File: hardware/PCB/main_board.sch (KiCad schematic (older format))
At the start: 0 parts

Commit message: update pcb,
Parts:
- added J?: TTL_UART, symbol Connector_Generic:Conn_01x03
- added J?: DPS1_UART, symbol Connector_Generic:Conn_01x03
- added J?: DPS2_UART, symbol Connector_Generic:Conn_01x03
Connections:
- net GND: now also J?.1 (Pin_1), J?.1 (Pin_1), J?.1 (Pin_1)
- new net licheepi_nano/UART0_RX: J?.3 (Pin_3)
- new net licheepi_nano/UART0_TX: J?.2 (Pin_2)
- new net licheepi_nano/UART1_RX: J?.3 (Pin_3)
- new net licheepi_nano/UART1_TX: J?.2 (Pin_2)
- new net licheepi_nano/UART2_RX: J?.3 (Pin_3)
- new net licheepi_nano/UART2_TX: J?.2 (Pin_2)
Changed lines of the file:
@@
 $Descr A4 11693 8268
 encoding utf-8
-Sheet 1 4
+Sheet 1 5
 Title ""
 Date ""
@@
 $EndDescr
 $Comp
-L customized_power:+5V #PWR?
+L customized_power:+5V #PWR0101
 U 1 1 5E8767E8
 P 950 1000
-F 0 "#PWR?" H 950 850 50  0001 C CNN
+F 0 "#PWR0101" H 950 850 50  0001 C CNN
 F 1 "+5V" H 965 1173 50  0000 C CNN
 F 2 "" H 950 1000 50  0001 C CNN
@@
 $EndComp
 $Comp
-L power:GND #PWR?
+L power:GND #PWR0102
 U 1 1 5E876DA9
 P 950 1300
-F 0 "#PWR?" H 950 1050 50  0001 C CNN
+F 0 "#PWR0102" H 950 1050 50  0001 C CNN
 F 1 "GND" H 955 1127 50  0000 C CNN
 F 2 "" H 950 1300 50  0001 C CNN
@@
 	1    0    0    -1
 $EndComp
-$Sheet
-S 4500 2400 1400 1050
+Entry Wire Line
+	3450 3150 3550 3050
+Entry Wire Line
+	3450 3050 3550 2950
+Entry Wire Line
+	3450 2950 3550 2850
+Entry Wire Line
+	3450 2850 3550 2750
+Entry Wire Line
+	3450 2750 3550 2650
+Entry Wire Line
+	3450 2650 3550 2550
+Wire Bus Line
+	3550 2300 4150 2300
+Entry Wire Line
+	4150 2550 4250 2650
+Entry Wire Line
+	4150 2650 4250 2750
+Entry Wire Line
+	4150 2750 4250 2850
+Entry Wire Line
+	4150 2850 4250 2950
+Entry Wire Line
+	4150 2950 4250 3050
+Entry Wire Line
+	4150 3050 4250 3150
+Wire Wire Line
+	4250 2650 4800 2650
+Wire Wire Line
+	4250 2750 4800 2750
+Wire Wire Line
+	4250 2850 4800 2850
+Wire Wire Line
+	4250 2950 4800 2950
+Wire Wire Line
+	4250 3050 4800 3050
+Wire Wire Line
+	4250 3150 4800 3150
+Wire Wire Line
+	2900 3150 3450 3150
+Wire Wire Line
+	2900 2650 3450 2650
+Wire Wire Line
+	2900 2750 3450 2750
+Wire Wire Line
+	2900 2850 3450 2850
+Wire Wire Line
+	2900 2950 3450 2950
+Wire Wire Line
+	2900 3050 3450 3050
+$Sheet
+S 1500 2400 1400 1050
+U 5E8B2717
+F0 "wifi" 50
+F1 "wifi.sch" 50
+F2 "SDC1_D2" B R 2900 3050 50
+F3 "SDC1_D1" B R 2900 2950 50
+F4 "SDC1_D0" B R 2900 2850 50
+F5 "SDC1_CLK" B R 2900 2750 50
+F6 "SDC1_CMD" B R 2900 2650 50
+F7 "SDC1_D3" B R 2900 3150 50
+$EndSheet
+Text Label 3000 2650 0    50   ~ 0
+SDC1_CMD
+Text Label 3000 2750 0    50   ~ 0
+SDC1_CLK
+Text Label 3000 2850 0    50   ~ 0
+SDC1_D0
+Text Label 3000 2950 0    50   ~ 0
+SDC1_D1
+Text Label 3000 3050 0    50   ~ 0
+SDC1_D2
+Text Label 3000 3150 0    50   ~ 0
+SDC1_D3
+Text Label 4350 2650 0    50   ~ 0
+SDC1_CMD
+Text Label 4350 2750 0    50   ~ 0
+SDC1_CLK
+Text Label 4350 2850 0    50   ~ 0
+SDC1_D0
+Text Label 4350 2950 0    50   ~ 0
+SDC1_D1
+Text Label 4350 3050 0    50   ~ 0
+SDC1_D2
+Text Label 4350 3150 0    50   ~ 0
+SDC1_D3
+$Sheet
+S 8450 4650 1600 1300
+U 5E91CDD8
+F0 "buzzer" 50
+F1 "buzzer.sch" 50
+F2 "BUZZER_OUTPUT" I L 8450 5150 50
+$EndSheet
+Wire Wire Line
+	7050 2600 8450 2600
+Wire Wire Line
+	7050 2800 8450 2800
+Wire Wire Line
+	7050 2900 8450 2900
+Wire Wire Line
+	7050 3000 8450 3000
+$Sheet
+S 8450 2400 1600 1050
+U 5E87CEF1
+F0 "gpio" 50
+F1 "gpio.sch" 50
+F2 "FEL" O L 8450 2600 50
+F3 "USER_BTN1" O L 8450 2800 50
+F4 "USER_BTN2" O L 8450 2900 50
+F5 "USER_BTN3" O L 8450 3000 50
+$EndSheet
+Wire Wire Line
+	7050 3900 7700 3900
+Wire Wire Line
+	7700 3900 7700 5150
+Wire Wire Line
+	7700 5150 8450 5150
+$Sheet
+S 4800 2400 2250 2250
 U 5E87A116
 F0 "licheepi_nano" 50
 F1 "licheepi_nano.sch" 50
-$EndSheet
-$Sheet
-S 6850 2400 1600 1050
-U 5E87CEF1
-F0 "gpio" 50
-F1 "gpio.sch" 50
-$EndSheet
-$Sheet
-S 2200 2400 1400 1050
-U 5E8B2717
-F0 "wifi" 50
-F1 "wifi.sch" 50
-$EndSheet
+F2 "SDC1_D2" B L 4800 3050 50
+F3 "SDC1_D1" B L 4800 2950 50
+F4 "SDC1_D0" B L 4800 2850 50
+F5 "SDC1_CLK" B L 4800 2750 50
+F6 "SDC1_CMD" B L 4800 2650 50
+F7 "SDC1_D3" B L 4800 3150 50
+F8 "FEL_ENABLE" I R 7050 2600 50
+F9 "PE2" I R 7050 2800 50
+F10 "PE3" I R 7050 2900 50
+F11 "PE4" I R 7050 3000 50
+F12 "PE5" O R 7050 3900 50
+F13 "UART0_TX" I L 4800 3450 50
+F14 "UART0_RX" I L 4800 3550 50
+F15 "UART1_TX" I L 4800 3800 50
+F16 "UART1_RX" I L 4800 3900 50
+F17 "UART2_RX" I L 4800 4250 50
+F18 "UART2_TX" I L 4800 4150 50
+$EndSheet
+$Comp
+L Connector_Generic:Conn_01x03 J?
+U 1 1 5E949A7D
+P 3750 3450
+F 0 "J?" H 3668 3767 50  0000 C CNN
+F 1 "TTL_UART" H 3668 3676 50  0000 C CNN
+F 2 "" H 3750 3450 50  0001 C CNN
+F 3 "~" H 3750 3450 50  0001 C CNN
+	1    3750 3450
+	-1   0    0    -1
+$EndComp
+$Comp
+L power:GND #PWR?
+U 1 1 5E94A27E
+P 4200 3350
+F 0 "#PWR?" H 4200 3100 50  0001 C CNN
+F 1 "GND" V 4205 3222 50  0000 R CNN
+F 2 "" H 4200 3350 50  0001 C CNN
+F 3 "" H 4200 3350 50  0001 C CNN
+	1    4200 3350
+	0    -1   -1   0
+$EndComp
+Wire Wire Line
+	3950 3350 4200 3350
+Wire Wire Line
+	3950 3450 4800 3450
+Wire Wire Line
+	3950 3550 4800 3550
+$Comp
+L Connector_Generic:Conn_01x03 J?
+U 1 1 5E94B27C
+P 3750 3800
+F 0 "J?" H 3829 3842 50  0000 L CNN
+F 1 "DPS1_UART" H 3829 3751 50  0000 L CNN
+F 2 "" H 3750 3800 50  0001 C CNN
+F 3 "~" H 3750 3800 50  0001 C CNN
+	1    3750 3800
+	-1   0    0    -1
+$EndComp
+$Comp
+L power:GND #PWR?
+U 1 1 5E94B286
+P 4200 3700
+F 0 "#PWR?" H 4200 3450 50  0001 C CNN
+F 1 "GND" V 4205 3572 50  0000 R CNN
+F 2 "" H 4200 3700 50  0001 C CNN
+F 3 "" H 4200 3700 50  0001 C CNN
+	1    4200 3700
+	0    -1   -1   0
+$EndComp
+Wire Wire Line
+	3950 3700 4200 3700
+Wire Wire Line
+	3950 3800 4800 3800
+Wire Wire Line
+	3950 3900 4800 3900
+$Comp
+L Connector_Generic:Conn_01x03 J?
+U 1 1 5E94C724
+P 3750 4150
+F 0 "J?" H 3829 4192 50  0000 L CNN
+F 1 "DPS2_UART" H 3829 4101 50  0000 L CNN
+F 2 "" H 3750 4150 50  0001 C CNN
+F 3 "~" H 3750 4150 50  0001 C CNN
+	1    3750 4150
+	-1   0    0    -1
+$EndComp
+$Comp
+L power:GND #PWR?
+U 1 1 5E94C72E
+P 4200 4050
+F 0 "#PWR?" H 4200 3800 50  0001 C CNN
+F 1 "GND" V 4205 3922 50  0000 R CNN
+F 2 "" H 4200 4050 50  0001 C CNN
+F 3 "" H 4200 4050 50  0001 C CNN
+	1    4200 4050
+	0    -1   -1   0
+$EndComp
+Wire Wire Line
+	3950 4050 4200 4050
+Wire Wire Line
+	3950 4150 4800 4150
+Wire Wire Line
+	3950 4250 4800 4250
+Wire Bus Line
+	3550 2300 3550 3050
+Wire Bus Line
+	4150 2300 4150 3050
 $EndSCHEMATC

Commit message: update before change,
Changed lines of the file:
@@
 $Descr A4 11693 8268
 encoding utf-8
-Sheet 1 5
+Sheet 1 6
 Title ""
 Date ""
@@
 SDC1_D3
 $Sheet
-S 8450 4650 1600 1300
+S 8400 3700 950  800
 U 5E91CDD8
 F0 "buzzer" 50
 F1 "buzzer.sch" 50
-F2 "BUZZER_OUTPUT" I L 8450 5150 50
+F2 "BUZZER_OUTPUT" I L 8400 4200 50
 $EndSheet
 Wire Wire Line
@@
 	7050 3900 7700 3900
 Wire Wire Line
-	7700 3900 7700 5150
-Wire Wire Line
-	7700 5150 8450 5150
-$Sheet
-S 4800 2400 2250 2250
+	7700 3900 7700 4200
+Wire Wire Line
+	7700 4200 8400 4200
+$Sheet
+S 4800 2400 2250 3200
 U 5E87A116
 F0 "licheepi_nano" 50
@@
 F17 "UART2_RX" I L 4800 4250 50
 F18 "UART2_TX" I L 4800 4150 50
+F19 "I2C0-SCK" B R 7050 4650 50
+F20 "I2C0-SDA" B R 7050 4750 50
+F21 "SPI0_CS" I R 7050 5100 50
+F22 "SPI0_MOSI" I R 7050 5200 50
+F23 "SPI0_CLK" I R 7050 5300 50
+F24 "SPI0_MISO" I R 7050 5400 50
 $EndSheet
 $Comp
@@
 	-1   0    0    -1
 $EndComp
+Wire Wire Line
+	3950 3450 4800 3450
+Wire Wire Line
+	3950 3550 4800 3550
+$Comp
+L Connector_Generic:Conn_01x03 J?
+U 1 1 5E94B27C
+P 3750 3800
+F 0 "J?" H 3829 3842 50  0000 L CNN
+F 1 "DPS1_UART" H 3829 3751 50  0000 L CNN
+F 2 "" H 3750 3800 50  0001 C CNN
+F 3 "~" H 3750 3800 50  0001 C CNN
+	1    3750 3800
+	-1   0    0    -1
+$EndComp
+$Comp
+L power:GND #PWR?
+U 1 1 5E94B286
+P 4200 3700
+F 0 "#PWR?" H 4200 3450 50  0001 C CNN
+F 1 "GND" V 4205 3572 50  0000 R CNN
+F 2 "" H 4200 3700 50  0001 C CNN
+F 3 "" H 4200 3700 50  0001 C CNN
+	1    4200 3700
+	0    -1   -1   0
+$EndComp
+Wire Wire Line
+	3950 3700 4200 3700
+Wire Wire Line
+	3950 3800 4800 3800
+Wire Wire Line
+	3950 3900 4800 3900
+$Comp
+L Connector_Generic:Conn_01x03 J?
+U 1 1 5E94C724
+P 3750 4150
+F 0 "J?" H 3829 4192 50  0000 L CNN
+F 1 "DPS2_UART" H 3829 4101 50  0000 L CNN
+F 2 "" H 3750 4150 50  0001 C CNN
+F 3 "~" H 3750 4150 50  0001 C CNN
+	1    3750 4150
+	-1   0    0    -1
+$EndComp
+$Comp
+L power:GND #PWR?
+U 1 1 5E94C72E
+P 4200 4050
+F 0 "#PWR?" H 4200 3800 50  0001 C CNN
+F 1 "GND" V 4205 3922 50  0000 R CNN
+F 2 "" H 4200 4050 50  0001 C CNN
+F 3 "" H 4200 4050 50  0001 C CNN
+	1    4200 4050
+	0    -1   -1   0
+$EndComp
+Wire Wire Line
+	3950 4050 4200 4050
+Wire Wire Line
+	3950 4150 4800 4150
+Wire Wire Line
+	3950 4250 4800 4250
+$Sheet
+S 9300 5000 950  1150
+U 5E8E2BE1
+F0 "terminals" 50
+F1 "terminals.sch" 50
+$EndSheet
+Wire Bus Line
+	7650 6150 8500 6150
+Wire Bus Line
+	8500 6150 8500 5050
+Entry Wire Line
+	7550 4650 7650 4750
+Entry Wire Line
+	7550 4750 7650 4850
+Entry Wire Line
+	7550 5100 7650 5200
+Entry Wire Line
+	7550 5200 7650 5300
+Entry Wire Line
+	7550 5300 7650 5400
+Entry Wire Line
+	7550 5400 7650 5500
+Wire Wire Line
+	7050 4650 7550 4650
+Wire Wire Line
+	7050 4750 7550 4750
+Wire Wire Line
+	7050 5100 7550 5100
+Wire Wire Line
+	7050 5200 7550 5200
+Wire Wire Line
+	7050 5300 7550 5300
+Wire Wire Line
+	7050 5400 7550 5400
+Text Label 7500 4650 2    50   ~ 0
+I2C0-SCK
+Text Label 7500 4750 2    50   ~ 0
+I2C0-SDA
+Text Label 7500 5100 2    50   ~ 0
+SPI0_CS
+Text Label 7500 5200 2    50   ~ 0
+SPI0_MOSI
+Text Label 7500 5300 2    50   ~ 0
+SPI0_CLK
+Text Label 7500 5400 2    50   ~ 0
+SPI0_MISO
+Wire Bus Line
+	7650 4550 7650 6150
+Wire Bus Line
+	4150 2300 4150 3050
+Wire Bus Line
+	3550 2300 3550 3050
+Wire Wire Line
+	3950 3350 4200 3350
 $Comp
 L power:GND #PWR?
@@
 	0    -1   -1   0
 $EndComp
-Wire Wire Line
-	3950 3350 4200 3350
-Wire Wire Line
-	3950 3450 4800 3450
-Wire Wire Line
-	3950 3550 4800 3550
-$Comp
-L Connector_Generic:Conn_01x03 J?
-U 1 1 5E94B27C
-P 3750 3800
-F 0 "J?" H 3829 3842 50  0000 L CNN
-F 1 "DPS1_UART" H 3829 3751 50  0000 L CNN
-F 2 "" H 3750 3800 50  0001 C CNN
-F 3 "~" H 3750 3800 50  0001 C CNN
-	1    3750 3800
-	-1   0    0    -1
-$EndComp
-$Comp
-L power:GND #PWR?
-U 1 1 5E94B286
-P 4200 3700
-F 0 "#PWR?" H 4200 3450 50  0001 C CNN
-F 1 "GND" V 4205 3572 50  0000 R CNN
-F 2 "" H 4200 3700 50  0001 C CNN
-F 3 "" H 4200 3700 50  0001 C CNN
-	1    4200 3700
-	0    -1   -1   0
-$EndComp
-Wire Wire Line
-	3950 3700 4200 3700
-Wire Wire Line
-	3950 3800 4800 3800
-Wire Wire Line
-	3950 3900 4800 3900
-$Comp
-L Connector_Generic:Conn_01x03 J?
-U 1 1 5E94C724
-P 3750 4150
-F 0 "J?" H 3829 4192 50  0000 L CNN
-F 1 "DPS2_UART" H 3829 4101 50  0000 L CNN
-F 2 "" H 3750 4150 50  0001 C CNN
-F 3 "~" H 3750 4150 50  0001 C CNN
-	1    3750 4150
-	-1   0    0    -1
-$EndComp
-$Comp
-L power:GND #PWR?
-U 1 1 5E94C72E
-P 4200 4050
-F 0 "#PWR?" H 4200 3800 50  0001 C CNN
-F 1 "GND" V 4205 3922 50  0000 R CNN
-F 2 "" H 4200 4050 50  0001 C CNN
-F 3 "" H 4200 4050 50  0001 C CNN
-	1    4200 4050
-	0    -1   -1   0
-$EndComp
-Wire Wire Line
-	3950 4050 4200 4050
-Wire Wire Line
-	3950 4150 4800 4150
-Wire Wire Line
-	3950 4250 4800 4250
-Wire Bus Line
-	3550 2300 3550 3050
-Wire Bus Line
-	4150 2300 4150 3050
 $EndSCHEMATC

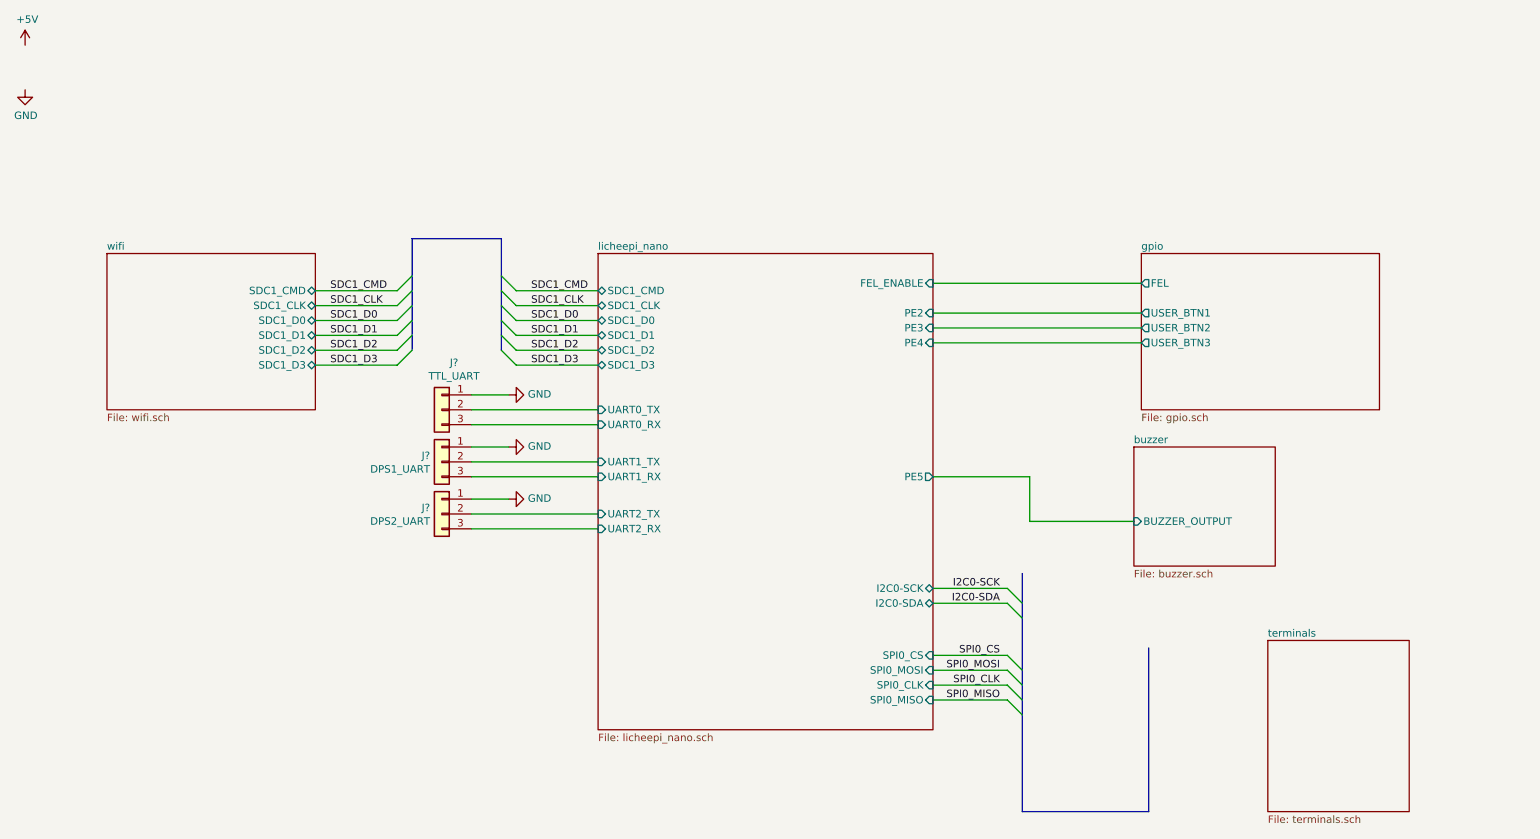
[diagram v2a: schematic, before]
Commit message: update for adding usb ttl converter,
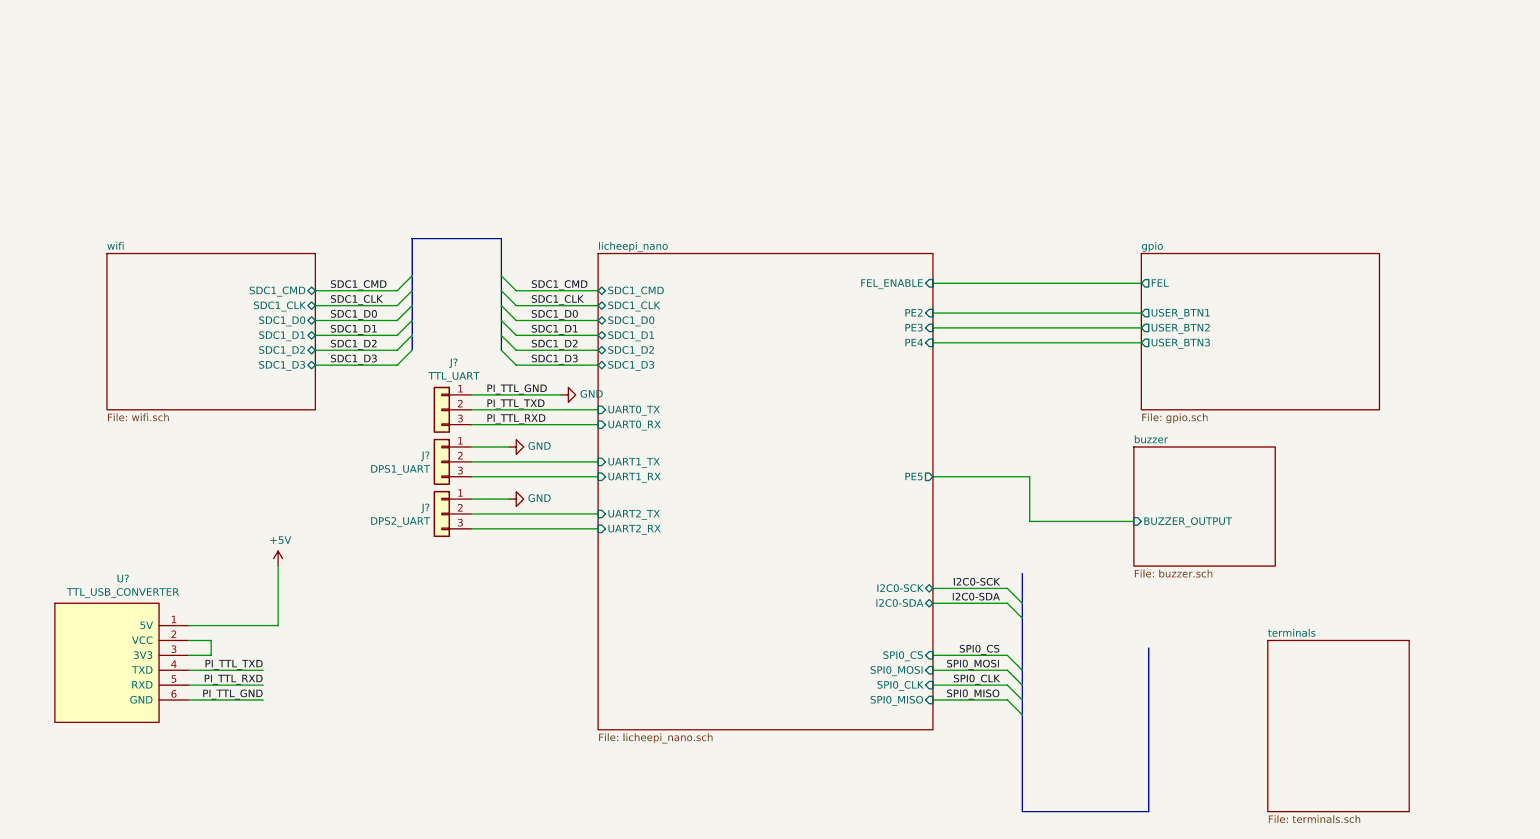
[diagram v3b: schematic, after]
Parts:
- added U?: TTL_USB_CONVERTER, footprint-lib:TTL_USB_CONVERTER, symbol taobao-components:TTL_USB_CONVERTER
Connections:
- net +5V: now also U?.1 (5V)
- net GND: now also U?.6 (GND)
- net licheepi_nano/UART0_RX renamed PI_TTL_RXD
- net PI_TTL_RXD: now also U?.5 (RXD)
- net licheepi_nano/UART0_TX renamed PI_TTL_TXD
- net PI_TTL_TXD: now also U?.4 (TXD)
- new net: U?.2 (VCC), U?.3 (3V3)
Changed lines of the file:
@@
 Comment4 ""
 $EndDescr
-$Comp
-L customized_power:+5V #PWR0101
-U 1 1 5E8767E8
-P 950 1000
-F 0 "#PWR0101" H 950 850 50  0001 C CNN
-F 1 "+5V" H 965 1173 50  0000 C CNN
-F 2 "" H 950 1000 50  0001 C CNN
-F 3 "" H 950 1000 50  0001 C CNN
-	1    950  1000
-	1    0    0    -1
-$EndComp
-$Comp
-L power:GND #PWR0102
-U 1 1 5E876DA9
-P 950 1300
-F 0 "#PWR0102" H 950 1050 50  0001 C CNN
-F 1 "GND" H 955 1127 50  0000 C CNN
-F 2 "" H 950 1300 50  0001 C CNN
-F 3 "" H 950 1300 50  0001 C CNN
-	1    950  1300
-	1    0    0    -1
-$EndComp
 Entry Wire Line
 	3450 3150 3550 3050
@@
 Text Label 7500 5400 2    50   ~ 0
 SPI0_MISO
-Wire Bus Line
-	7650 4550 7650 6150
-Wire Bus Line
-	4150 2300 4150 3050
-Wire Bus Line
-	3550 2300 3550 3050
-Wire Wire Line
-	3950 3350 4200 3350
+Wire Wire Line
+	3950 3350 4550 3350
 $Comp
 L power:GND #PWR?
 U 1 1 5E94A27E
-P 4200 3350
-F 0 "#PWR?" H 4200 3100 50  0001 C CNN
-F 1 "GND" V 4205 3222 50  0000 R CNN
-F 2 "" H 4200 3350 50  0001 C CNN
-F 3 "" H 4200 3350 50  0001 C CNN
-	1    4200 3350
+P 4550 3350
+F 0 "#PWR?" H 4550 3100 50  0001 C CNN
+F 1 "GND" V 4555 3222 50  0000 R CNN
+F 2 "" H 4550 3350 50  0001 C CNN
+F 3 "" H 4550 3350 50  0001 C CNN
+	1    4550 3350
 	0    -1   -1   0
 $EndComp
+$Comp
+L taobao-components:TTL_USB_CONVERTER U?
+U 1 1 5E991FE4
+P 1500 5150
+F 0 "U?" H 1608 5715 50  0000 C CNN
+F 1 "TTL_USB_CONVERTER" H 1608 5624 50  0000 C CNN
+F 2 "footprint-lib:TTL_USB_CONVERTER" H 1500 5150 50  0001 C CNN
+F 3 "" H 1500 5150 50  0001 C CNN
+	1    1500 5150
+	1    0    0    -1
+$EndComp
+Text Label 4050 3350 0    50   ~ 0
+PI_TTL_GND
+Text Label 4050 3450 0    50   ~ 0
+PI_TTL_TXD
+Text Label 4050 3550 0    50   ~ 0
+PI_TTL_RXD
+Text Label 2550 5400 2    50   ~ 0
+PI_TTL_GND
+Text Label 2550 5200 2    50   ~ 0
+PI_TTL_TXD
+Text Label 2550 5300 2    50   ~ 0
+PI_TTL_RXD
+Wire Wire Line
+	2050 5200 2550 5200
+Wire Wire Line
+	2050 5300 2550 5300
+Wire Wire Line
+	2050 5400 2550 5400
+$Comp
+L customized_power:+5V #PWR?
+U 1 1 5E99CA17
+P 2650 4500
+F 0 "#PWR?" H 2650 4350 50  0001 C CNN
+F 1 "+5V" H 2665 4673 50  0000 C CNN
+F 2 "" H 2650 4500 50  0001 C CNN
+F 3 "" H 2650 4500 50  0001 C CNN
+	1    2650 4500
+	1    0    0    -1
+$EndComp
+Wire Wire Line
+	2650 4500 2650 4900
+Wire Wire Line
+	2650 4900 2050 4900
+Wire Wire Line
+	2050 5000 2200 5000
+Wire Wire Line
+	2200 5000 2200 5100
+Wire Wire Line
+	2200 5100 2050 5100
+Wire Bus Line
+	3550 2300 3550 3050
+Wire Bus Line
+	4150 2300 4150 3050
+Wire Bus Line
+	7650 4550 7650 6150
 $EndSCHEMATC

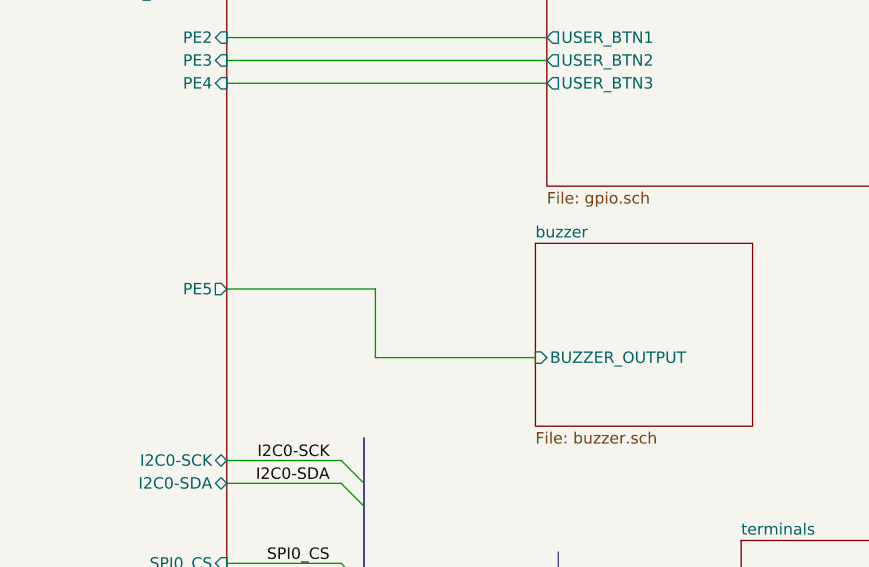
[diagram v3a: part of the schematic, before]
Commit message: sch: update buzzer connection,
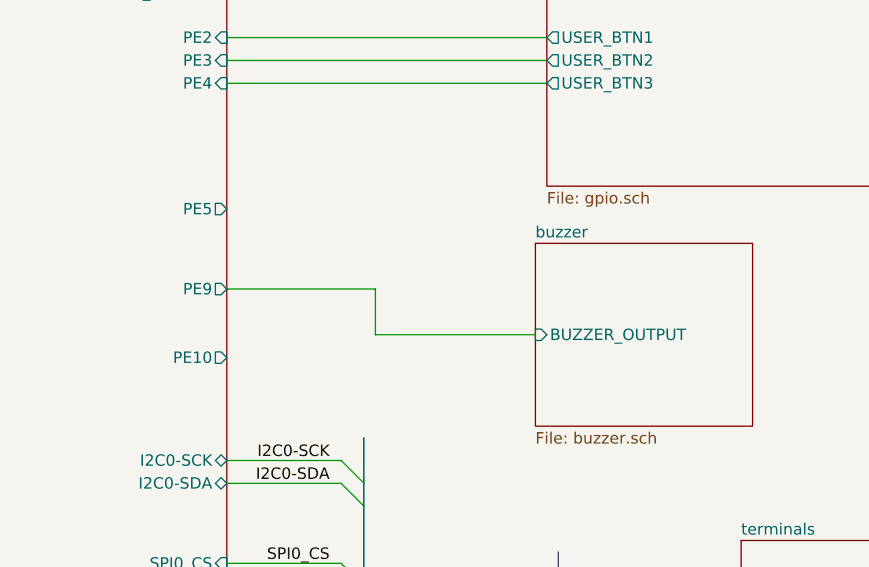
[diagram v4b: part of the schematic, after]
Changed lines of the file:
@@
 F0 "buzzer" 50
 F1 "buzzer.sch" 50
-F2 "BUZZER_OUTPUT" I L 8400 4200 50
+F2 "BUZZER_OUTPUT" I L 8400 4100 50
 $EndSheet
 Wire Wire Line
@@
 	7050 3900 7700 3900
 Wire Wire Line
-	7700 3900 7700 4200
+	7700 3900 7700 4100
 Wire Wire Line
-	7700 4200 8400 4200
+	7700 4100 8400 4100
 $Sheet
 S 4800 2400 2250 3200
@@
 F10 "PE3" I R 7050 2900 50
 F11 "PE4" I R 7050 3000 50
-F12 "PE5" O R 7050 3900 50
-F13 "UART0_TX" I L 4800 3450 50
-F14 "UART0_RX" I L 4800 3550 50
-F15 "UART1_TX" I L 4800 3800 50
-F16 "UART1_RX" I L 4800 3900 50
-F17 "UART2_RX" I L 4800 4250 50
-F18 "UART2_TX" I L 4800 4150 50
-F19 "I2C0-SCK" B R 7050 4650 50
-F20 "I2C0-SDA" B R 7050 4750 50
-F21 "SPI0_CS" I R 7050 5100 50
-F22 "SPI0_MOSI" I R 7050 5200 50
-F23 "SPI0_CLK" I R 7050 5300 50
-F24 "SPI0_MISO" I R 7050 5400 50
+F12 "UART0_TX" I L 4800 3450 50
+F13 "UART0_RX" I L 4800 3550 50
+F14 "UART1_TX" I L 4800 3800 50
+F15 "UART1_RX" I L 4800 3900 50
+F16 "UART2_RX" I L 4800 4250 50
+F17 "UART2_TX" I L 4800 4150 50
+F18 "I2C0-SCK" B R 7050 4650 50
+F19 "I2C0-SDA" B R 7050 4750 50
+F20 "SPI0_CS" I R 7050 5100 50
+F21 "SPI0_MOSI" I R 7050 5200 50
+F22 "SPI0_CLK" I R 7050 5300 50
+F23 "SPI0_MISO" I R 7050 5400 50
+F24 "PE5" O R 7050 3550 50
+F25 "PE9" O R 7050 3900 50
+F26 "PE10" O R 7050 4200 50
 $EndSheet
 $Comp
